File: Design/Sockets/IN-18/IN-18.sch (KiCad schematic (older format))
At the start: 18 parts, among them J1 Conn_01x12_Male, J2 Conn_01x12_Male, J3 Conn_01x12_Male, J4 Conn_01x12_Male, J5 Conn_01x12_Male, J6 Conn_01x12_Male, U1 IN-18, U2 IN-18, U3 IN-18, U4 IN-18, U5 IN-18, U6 IN-18

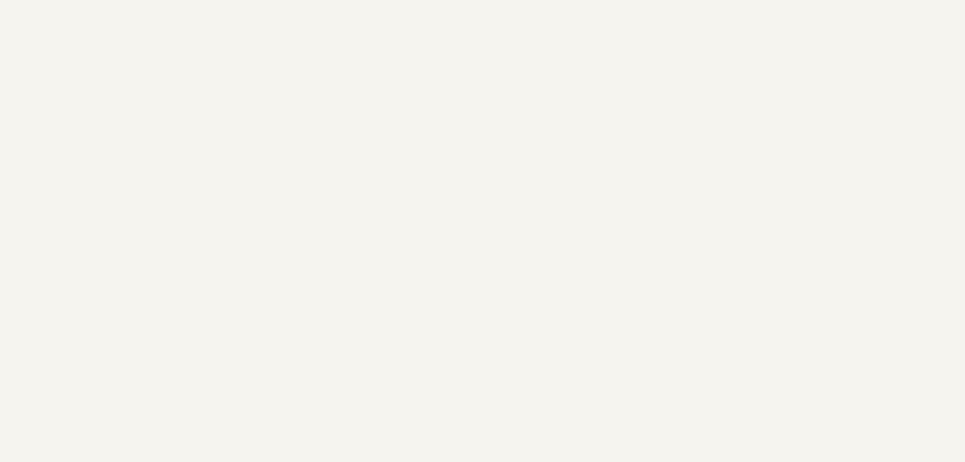
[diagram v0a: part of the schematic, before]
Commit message: Add license notice to all human readable files
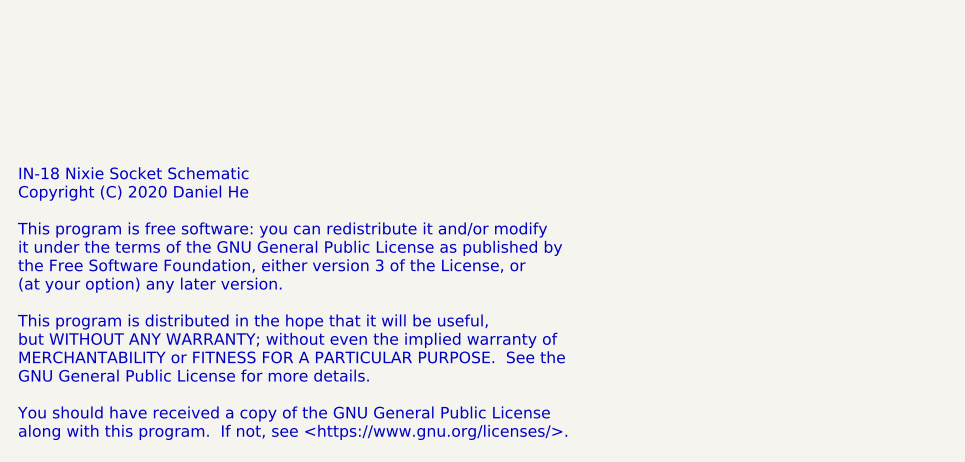
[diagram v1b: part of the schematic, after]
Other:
- note added: "IN-18 Nixie Socket Schematic\nCopyright (C) 2020 Daniel He\n\nThis program is free software: you can redistribute it and/or modify\nit under the terms of the GNU General Public License as published by\nthe Free Software Foundation, either version 3 of the License, or\n(at your option) any later version.\n\nThis program is distributed in the hope that it will be useful,\nbut WITHOUT ANY WARRANTY; 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"
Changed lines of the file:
@@
 Text GLabel 9850 3150 1    50   Input ~ 0
 HV
+Text Notes 550  7700 0    50   ~ 0
+IN-18 Nixie Socket Schematic\nCopyright (C) 2020 Daniel He\n\nThis program is free software: you can redistribute it and/or modify\nit under the terms of the GNU General Public License as published by\nthe Free Software Foundation, either version 3 of the License, or\n(at your option) any later version.\n\nThis program is distributed in the hope that it will be useful,\nbut WITHOUT ANY WARRANTY; without even the implied warranty of\nMERCHANTABILITY or FITNESS FOR A PARTICULAR PURPOSE.  See the\nGNU General Public License for more details.\n\nYou should have received a copy of the GNU General Public License\nalong with this program.  If not, see <https://www.gnu.org/licenses/>.
 $EndSCHEMATC
